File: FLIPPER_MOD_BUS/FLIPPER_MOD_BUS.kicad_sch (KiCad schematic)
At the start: 14 parts, among them J1 Conn_01x02, J2 Conn_01x10_Socket, J3 Conn_01x08_Socket, J4 Conn_01x02_Socket, U1 SP3485EN

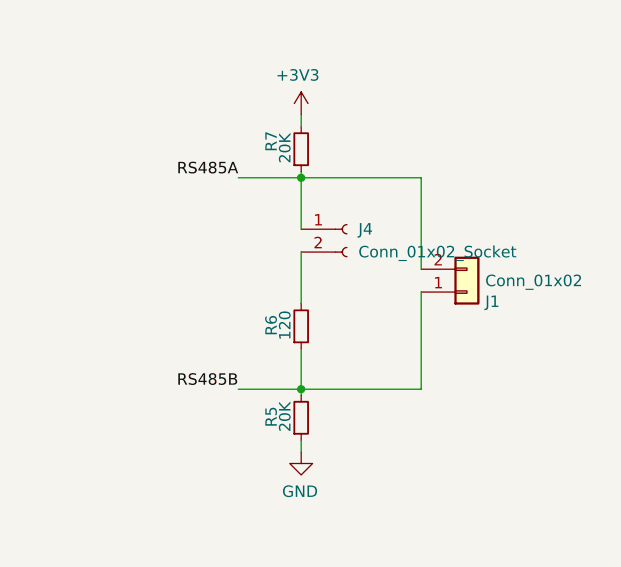
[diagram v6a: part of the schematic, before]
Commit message: fix(hw): Differential Pair
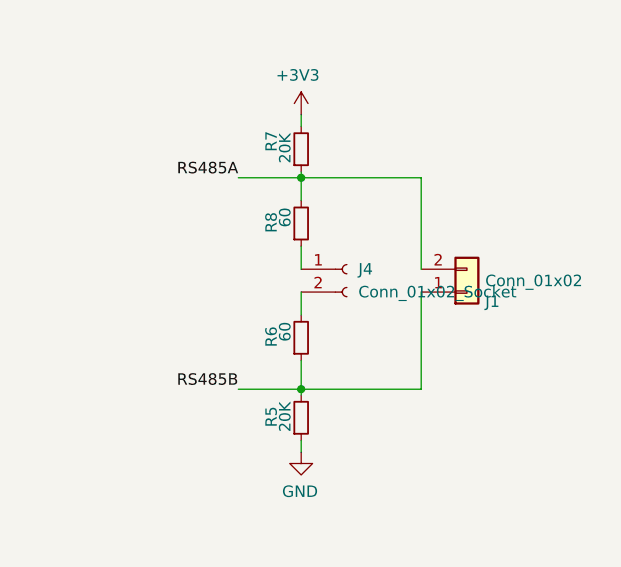
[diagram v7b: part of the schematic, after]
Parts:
- added R8: 60, Resistor_SMD:R_1206_3216Metric_Pad1.30x1.75mm_HandSolder, symbol Device:R_Small
- R6: value 120 -> 60; footprint Resistor_SMD:R_0603_1608Metric_Pad0.98x0.95mm_HandSolder -> Resistor_SMD:R_1206_3216Metric_Pad1.30x1.75mm_HandSolder; LCSC# C103256 -> (none); manf# RTT03121JTP -> 71-CRCW120660R0KNAIF
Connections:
- net RS485A: now also R8.2; no longer J4.1 (Pin_1)
- new net: J4.1 (Pin_1), R8.1
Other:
- moved on the sheet: J4, R6
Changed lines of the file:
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@@
+	(wire
+		(pts
+			(xy 148.59 31.75) (xy 148.59 32.385)
+		)
+		(stroke
+			(width 0)
+			(type default)
+		)
+	)
 	(wire
 		(pts
@@
 	(wire
 		(pts
-			(xy 148.59 51.435) (xy 148.59 55.88)
-		)
-		(stroke
-			(width 0)
-			(type default)
-		)
-	)
-	(wire
-		(pts
-			(xy 148.59 40.64) (xy 148.59 46.355)
+			(xy 148.59 52.705) (xy 148.59 55.88)
+		)
+		(stroke
+			(width 0)
+			(type default)
+		)
+	)
+	(wire
+		(pts
+			(xy 148.59 45.085) (xy 148.59 47.625)
 		)
 		(stroke
@@
 	(wire
 		(pts
-			(xy 148.59 32.385) (xy 148.59 38.1)
+			(xy 148.59 40.005) (xy 148.59 42.545)
 		)
 		(stroke
@@
 	(wire
 		(pts
+			(xy 148.59 32.385) (xy 148.59 34.925)
+		)
+		(stroke
+			(width 0)
+			(type default)
+		)
+	)
+	(wire
+		(pts
 			(xy 53.594 32.258) (xy 53.594 30.734)
 		)
@@
 		(pts
 			(xy 148.59 55.88) (xy 148.59 56.515)
-		)
-		(stroke
-			(width 0)
-			(type default)
-		)
-	)
-	(wire
-		(pts
-			(xy 148.59 31.75) (xy 148.59 32.385)
 		)
 		(stroke
@@
 	(symbol
 		(lib_id "Device:R_Small")
-		(at 148.59 48.895 0)
+		(at 148.59 50.165 0)
 		(mirror x)
 		(unit 1)
@@
 		(dnp no)
 		(property "Reference" "R6"
-			(at 145.288 47.625 90)
+			(at 145.288 48.895 90)
 			(effects
 				(font
@@
 			)
 		)
-		(property "Value" "120"
-			(at 146.812 47.117 90)
+		(property "Value" "60"
+			(at 146.812 48.387 90)
 			(effects
 				(font
@@
 			)
 		)
-		(property "Footprint" "Resistor_SMD:R_0603_1608Metric_Pad0.98x0.95mm_HandSolder"
-			(at 148.59 48.895 0)
+		(property "Footprint" "Resistor_SMD:R_1206_3216Metric_Pad1.30x1.75mm_HandSolder"
+			(at 148.59 50.165 0)
 			(effects
 				(font
@@
 		)
 		(property "Datasheet" "https://lcsc.com/product-detail/Chip-Resistor-Surface-Mount_120R-121-5_C103256.html"
-			(at 148.59 48.895 0)
+			(at 148.59 50.165 0)
 			(effects
 				(font
@@
 		)
 		(property "Description" ""
-			(at 148.59 48.895 0)
-			(effects
-				(font
-					(size 1.27 1.27)
-				)
-				(hide yes)
-			)
-		)
-		(property "manf#" "RTT03121JTP"
-			(at 148.59 48.895 0)
-			(effects
-				(font
-					(size 1.27 1.27)
-				)
-				(hide yes)
-			)
-		)
-		(property "LCSC#" "C103256"
-			(at 148.59 48.895 0)
+			(at 148.59 50.165 0)
+			(effects
+				(font
+					(size 1.27 1.27)
+				)
+				(hide yes)
+			)
+		)
+		(property "manf#" "71-CRCW120660R0KNAIF "
+			(at 148.59 50.165 0)
+			(effects
+				(font
+					(size 1.27 1.27)
+				)
+				(hide yes)
+			)
+		)
+		(property "LCSC#" ""
+			(at 148.59 50.165 0)
 			(effects
 				(font
@@
 		)
 		(property "Proveedor" "LCSC"
-			(at 148.59 48.895 0)
+			(at 148.59 50.165 0)
 			(effects
 				(font
@@
 	(symbol
 		(lib_id "Connector:Conn_01x02_Socket")
-		(at 153.67 38.1 0)
+		(at 153.67 42.545 0)
 		(unit 1)
 		(exclude_from_sim no)
@@
 		(fields_autoplaced yes)
 		(property "Reference" "J4"
-			(at 154.94 38.1 0)
+			(at 154.94 42.545 0)
 			(effects
 				(font
@@
 		)
 		(property "Value" "Conn_01x02_Socket"
-			(at 154.94 40.64 0)
+			(at 154.94 45.085 0)
 			(effects
 				(font
@@
 		)
 		(property "Footprint" "Connector_PinHeader_2.54mm:PinHeader_1x02_P2.54mm_Vertical"
-			(at 153.67 38.1 0)
+			(at 153.67 42.545 0)
 			(effects
 				(font
@@
 		)
 		(property "Datasheet" "https://www.lcsc.com/datasheet/lcsc_datasheet_2401281145_XUNPU-PH2-54-01-02PZD_C7501580.pdf"
-			(at 153.67 38.1 0)
+			(at 153.67 42.545 0)
 			(effects
 				(font
@@
 		)
 		(property "Description" ""
-			(at 153.67 38.1 0)
+			(at 153.67 42.545 0)
 			(effects
 				(font
@@
 		)
 		(property "LCSC#" "C7501580"
-			(at 153.67 38.1 0)
+			(at 153.67 42.545 0)
 			(effects
 				(font
@@
 		)
 		(property "Manufactura" "LCSC"
-			(at 153.67 38.1 0)
+			(at 153.67 42.545 0)
 			(effects
 				(font
@@
 		)
 		(property "manf#" "PH2.54-01-02PZD"
-			(at 153.67 38.1 0)
+			(at 153.67 42.545 0)
 			(effects
 				(font
@@
 					(unit 1)
 				)
+			)
+		)
+	)
+	(symbol
+		(lib_id "Device:R_Small")
+		(at 148.59 37.465 0)
+		(mirror x)
+		(unit 1)
+		(exclude_from_sim no)
+		(in_bom yes)
+		(on_board yes)
+		(dnp no)
+		(property "Reference" "R8"
+			(at 145.288 36.195 90)
+			(effects
+				(font
+					(size 1.27 1.27)
+				)
+				(justify left)
+			)
+		)
+		(property "Value" "60"
+			(at 146.812 35.687 90)
+			(effects
+				(font
+					(size 1.27 1.27)
+				)
+				(justify left)
+			)
+		)
+		(property "Footprint" "Resistor_SMD:R_1206_3216Metric_Pad1.30x1.75mm_HandSolder"
+			(at 148.59 37.465 0)
+			(effects
+				(font
+					(size 1.27 1.27)
+				)
+				(hide yes)
+			)
+		)
+		(property "Datasheet" "https://lcsc.com/product-detail/Chip-Resistor-Surface-Mount_120R-121-5_C103256.html"
+			(at 148.59 37.465 0)
+			(effects
+				(font
+					(size 1.27 1.27)
+				)
+				(hide yes)
+			)
+		)
+		(property "Description" ""
+			(at 148.59 37.465 0)
+			(effects
+				(font
+					(size 1.27 1.27)
+				)
+				(hide yes)
+			)
+		)
+		(property "manf#" "71-CRCW120660R0KNAIF "
+			(at 148.59 37.465 0)
+			(effects
+				(font
+					(size 1.27 1.27)
+				)
+				(hide yes)
+			)
+		)
+		(property "LCSC#" ""
+			(at 148.59 37.465 0)
+			(effects
+				(font
+					(size 1.27 1.27)
+				)
+				(hide yes)
+			)
+		)
+		(property "Proveedor" "LCSC"
+			(at 148.59 37.465 0)
+			(effects
+				(font
+					(size 1.27 1.27)
+				)
+				(hide yes)
+			)
+		)
+		(pin "1"
+		)
+		(pin "2"
+		)
+		(instances
+			(project "FLIPPER_MOD_BUS"
+				(path "/000d5789-2d2c-436e-a8f3-713f1968a92a"
+					(reference "R8")
+					(unit 1)
+				)
